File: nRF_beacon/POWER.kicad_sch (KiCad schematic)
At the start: 17 parts, among them U2 NPM1300-QEAA-R7

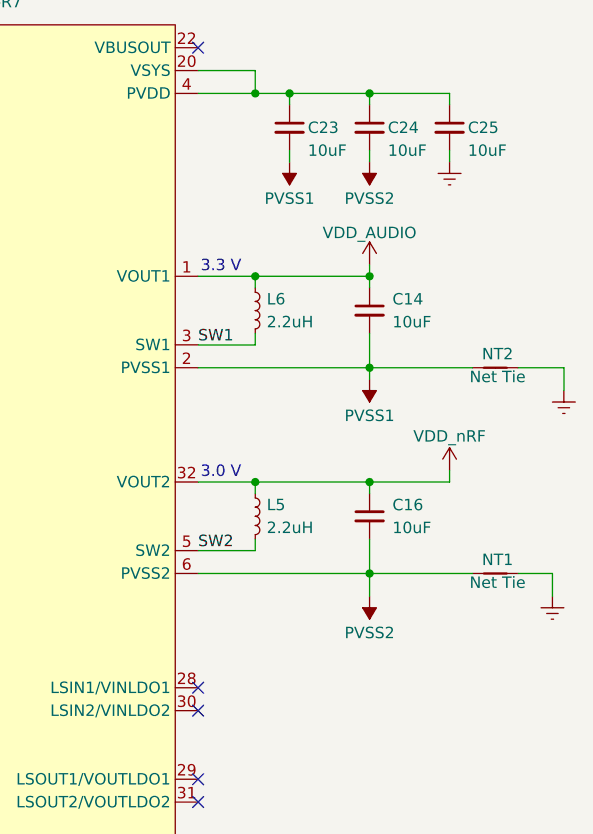
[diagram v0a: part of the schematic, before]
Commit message: Began typical application around nPM1300
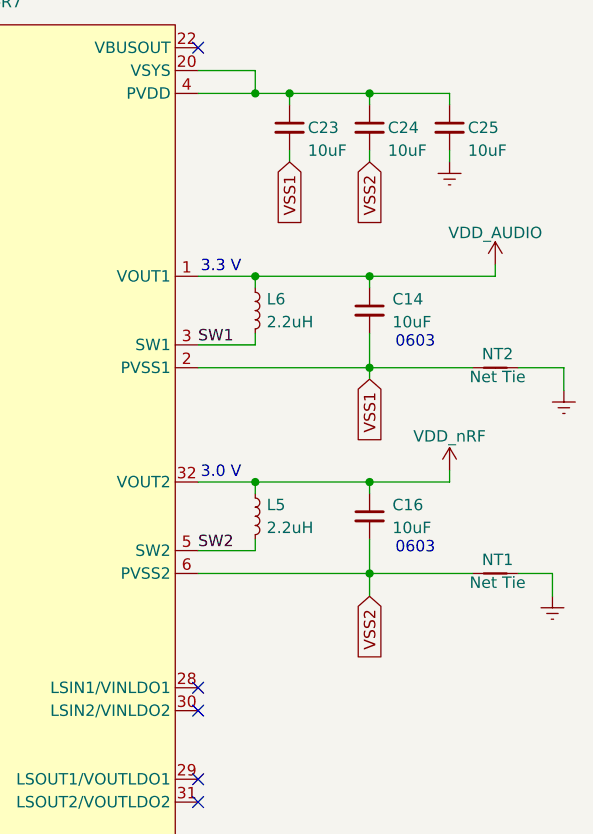
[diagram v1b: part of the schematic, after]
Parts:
- C14, C16: MPN KGM15CR51E106KT -> (none); Price 5.09 -> (none)
- NT1, NT2: footprint NetTie:NetTie-4_SMD_Pad0.5mm -> Ekse:NetTieSmall
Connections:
- net VSS1: now reaches C14.2, NT2.1, U2.2 (PVSS1)
- net VSS1: now also C23.2
- net VSS2: now reaches C16.2, NT1.1, U2.6 (PVSS2)
- net VSS2: now also C24.2
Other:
- note added: "0603"
